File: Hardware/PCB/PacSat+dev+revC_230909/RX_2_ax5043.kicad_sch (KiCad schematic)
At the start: 15 parts, among them U151 RFShield_OnePiece, U305 AX5043

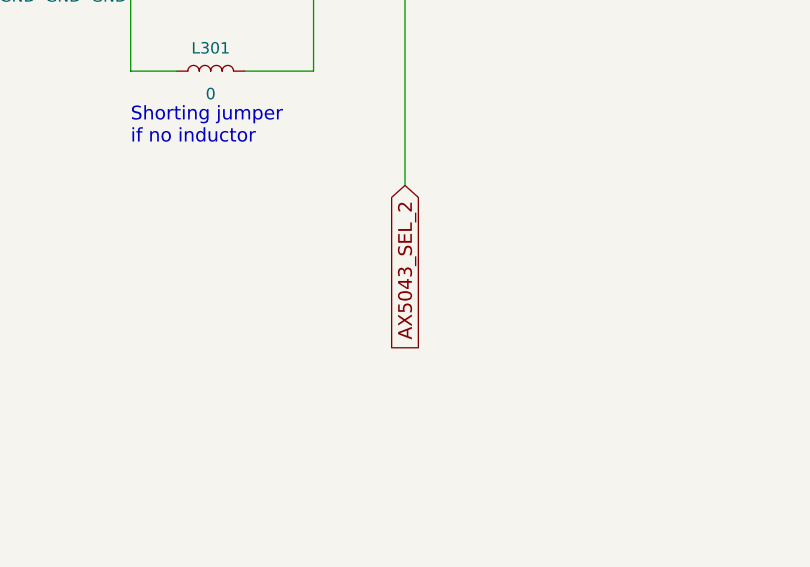
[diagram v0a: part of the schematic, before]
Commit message: Changed schematic to add Select lines for each AX5043 on the CPU.
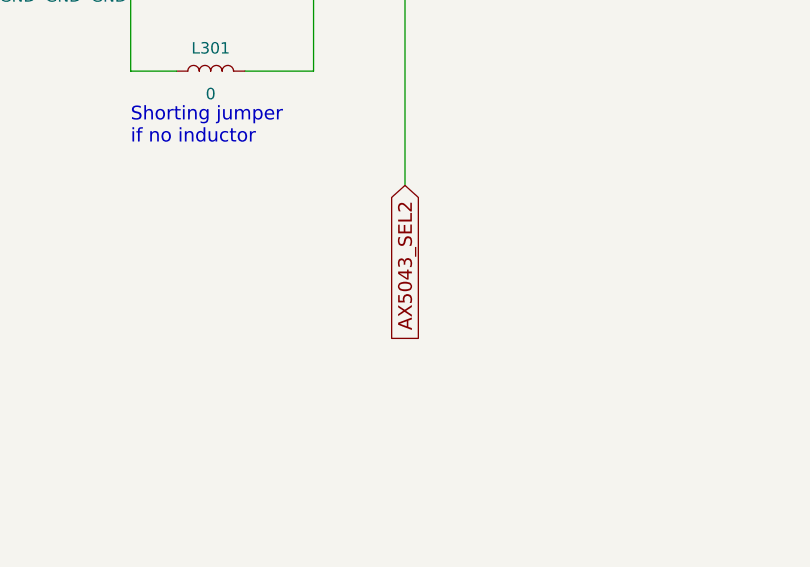
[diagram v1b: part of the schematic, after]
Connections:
- net AX5043_SEL_2 renamed AX5043_SEL2
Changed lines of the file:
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@@
     )
   )
-  (global_label "AX5043_SEL_2" (shape input) (at 226.06 181.61 270) (fields_autoplaced)
+  (global_label "AX5043_SEL2" (shape input) (at 226.06 181.61 270) (fields_autoplaced)
     (effects (font (size 1.524 1.524)) (justify right))
-    (property "Intersheetrefs" "${INTERSHEET_REFS}" (at 226.06 200.7123 90)
+    (property "Intersheetrefs" "${INTERSHEET_REFS}" (at 226.06 199.6466 90)
       (effects (font (size 1.524 1.524)) (justify right) hide)
     )
@@
     (pin "2")
     (instances
-      (project "pACsAT_dEV_rEVc_230907"
+      (project "PacSat+dev+revC_230909"
         (path "/cc9f42d2-6985-41ac-acab-5ab7b01c5b38/00000000-0000-0000-0000-00005a014be3"
           (reference "C712") (unit 1)
@@
     (pin "1")
     (instances
-      (project "pACsAT_dEV_rEVc_230907"
+      (project "PacSat+dev+revC_230909"
         (path "/cc9f42d2-6985-41ac-acab-5ab7b01c5b38/07d62cf1-e888-4b13-86c4-67d770627579"
           (reference "#PWR0191") (unit 1)
@@
     (pin "2")
     (instances
-      (project "pACsAT_dEV_rEVc_230907"
+      (project "PacSat+dev+revC_230909"
         (path "/cc9f42d2-6985-41ac-acab-5ab7b01c5b38/1e7123c2-80dc-43cd-b90a-12f3fe1af0cb"
           (reference "R303") (unit 1)
@@
     (pin "1")
     (instances
-      (project "pACsAT_dEV_rEVc_230907"
+      (project "PacSat+dev+revC_230909"
         (path "/cc9f42d2-6985-41ac-acab-5ab7b01c5b38/1e7123c2-80dc-43cd-b90a-12f3fe1af0cb"
           (reference "#PWR0304") (unit 1)
@@
     (pin "5")
     (instances
-      (project "pACsAT_dEV_rEVc_230907"
+      (project "PacSat+dev+revC_230909"
         (path "/cc9f42d2-6985-41ac-acab-5ab7b01c5b38/00000000-0000-0000-0000-00005a014be3"
           (reference "U151") (unit 1)
@@
     (pin "1")
     (instances
-      (project "pACsAT_dEV_rEVc_230907"
+      (project "PacSat+dev+revC_230909"
         (path "/cc9f42d2-6985-41ac-acab-5ab7b01c5b38/00000000-0000-0000-0000-00005a014be3"
           (reference "#PWR0161") (unit 1)
@@
     (pin "2")
     (instances
-      (project "pACsAT_dEV_rEVc_230907"
+      (project "PacSat+dev+revC_230909"
         (path "/cc9f42d2-6985-41ac-acab-5ab7b01c5b38/00000000-0000-0000-0000-00005a014be3"
           (reference "C711") (unit 1)
@@
     (pin "2")
     (instances
-      (project "pACsAT_dEV_rEVc_230907"
+      (project "PacSat+dev+revC_230909"
         (path "/cc9f42d2-6985-41ac-acab-5ab7b01c5b38/1e7123c2-80dc-43cd-b90a-12f3fe1af0cb"
           (reference "C303") (unit 1)
@@
     (pin "2")
     (instances
-      (project "pACsAT_dEV_rEVc_230907"
+      (project "PacSat+dev+revC_230909"
         (path "/cc9f42d2-6985-41ac-acab-5ab7b01c5b38/1e7123c2-80dc-43cd-b90a-12f3fe1af0cb"
           (reference "C304") (unit 1)
@@
     (pin "2")
     (instances
-      (project "pACsAT_dEV_rEVc_230907"
+      (project "PacSat+dev+revC_230909"
         (path "/cc9f42d2-6985-41ac-acab-5ab7b01c5b38/1e7123c2-80dc-43cd-b90a-12f3fe1af0cb"
           (reference "C307") (unit 1)
@@
     (pin "3")
     (instances
-      (project "pACsAT_dEV_rEVc_230907"
+      (project "PacSat+dev+revC_230909"
         (path "/cc9f42d2-6985-41ac-acab-5ab7b01c5b38/9af0eacb-5211-4e23-85d7-9c1805bbe6a4"
           (reference "U607") (unit 1)
@@
     (pin "1")
     (instances
-      (project "pACsAT_dEV_rEVc_230907"
+      (project "PacSat+dev+revC_230909"
         (path "/cc9f42d2-6985-41ac-acab-5ab7b01c5b38/1e7123c2-80dc-43cd-b90a-12f3fe1af0cb"
           (reference "#PWR0309") (unit 1)
@@
     (pin "1")
     (instances
-      (project "pACsAT_dEV_rEVc_230907"
+      (project "PacSat+dev+revC_230909"
         (path "/cc9f42d2-6985-41ac-acab-5ab7b01c5b38/1e7123c2-80dc-43cd-b90a-12f3fe1af0cb"
           (reference "#PWR0308") (unit 1)
@@
     (pin "1")
     (instances
-      (project "pACsAT_dEV_rEVc_230907"
+      (project "PacSat+dev+revC_230909"
         (path "/cc9f42d2-6985-41ac-acab-5ab7b01c5b38/00000000-0000-0000-0000-00005a014be3"
           (reference "#PWR0735") (unit 1)
@@
     (pin "1")
     (instances
-      (project "pACsAT_dEV_rEVc_230907"
+      (project "PacSat+dev+revC_230909"
         (path "/cc9f42d2-6985-41ac-acab-5ab7b01c5b38/1e7123c2-80dc-43cd-b90a-12f3fe1af0cb"
           (reference "#PWR0312") (unit 1)
@@
     (pin "2")
     (instances
-      (project "pACsAT_dEV_rEVc_230907"
+      (project "PacSat+dev+revC_230909"
         (path "/cc9f42d2-6985-41ac-acab-5ab7b01c5b38/1e7123c2-80dc-43cd-b90a-12f3fe1af0cb"
           (reference "C301") (unit 1)
@@
     (pin "9")
     (instances
-      (project "pACsAT_dEV_rEVc_230907"
+      (project "PacSat+dev+revC_230909"
         (path "/cc9f42d2-6985-41ac-acab-5ab7b01c5b38/1e7123c2-80dc-43cd-b90a-12f3fe1af0cb"
           (reference "U305") (unit 1)
@@
     (pin "1")
     (instances
-      (project "pACsAT_dEV_rEVc_230907"
+      (project "PacSat+dev+revC_230909"
         (path "/cc9f42d2-6985-41ac-acab-5ab7b01c5b38/1e7123c2-80dc-43cd-b90a-12f3fe1af0cb"
           (reference "#PWR0311") (unit 1)
@@
     (pin "3")
     (instances
-      (project "pACsAT_dEV_rEVc_230907"
+      (project "PacSat+dev+revC_230909"
         (path "/cc9f42d2-6985-41ac-acab-5ab7b01c5b38/9af0eacb-5211-4e23-85d7-9c1805bbe6a4"
           (reference "U605") (unit 1)
@@
     (pin "2")
     (instances
-      (project "pACsAT_dEV_rEVc_230907"
+      (project "PacSat+dev+revC_230909"
         (path "/cc9f42d2-6985-41ac-acab-5ab7b01c5b38/1e7123c2-80dc-43cd-b90a-12f3fe1af0cb"
           (reference "C302") (unit 1)
@@
     (pin "1")
     (instances
-      (project "pACsAT_dEV_rEVc_230907"
+      (project "PacSat+dev+revC_230909"
         (path "/cc9f42d2-6985-41ac-acab-5ab7b01c5b38/07d62cf1-e888-4b13-86c4-67d770627579"
           (reference "#PWR0191") (unit 1)
@@
     (pin "1")
     (instances
-      (project "pACsAT_dEV_rEVc_230907"
+      (project "PacSat+dev+revC_230909"
         (path "/cc9f42d2-6985-41ac-acab-5ab7b01c5b38/1e7123c2-80dc-43cd-b90a-12f3fe1af0cb"
           (reference "#PWR0305") (unit 1)
@@
     (pin "1")
     (instances
-      (project "pACsAT_dEV_rEVc_230907"
+      (project "PacSat+dev+revC_230909"
         (path "/cc9f42d2-6985-41ac-acab-5ab7b01c5b38/9af0eacb-5211-4e23-85d7-9c1805bbe6a4"
           (reference "#PWR0614") (unit 1)
@@
     (pin "2")
     (instances
-      (project "pACsAT_dEV_rEVc_230907"
+      (project "PacSat+dev+revC_230909"
         (path "/cc9f42d2-6985-41ac-acab-5ab7b01c5b38/07d62cf1-e888-4b13-86c4-67d770627579"
           (reference "R88") (unit 1)
@@
     (pin "2")
     (instances
-      (project "pACsAT_dEV_rEVc_230907"
+      (project "PacSat+dev+revC_230909"
         (path "/cc9f42d2-6985-41ac-acab-5ab7b01c5b38/1e7123c2-80dc-43cd-b90a-12f3fe1af0cb"
           (reference "R302") (unit 1)
@@
     (pin "1")
     (instances
-      (project "pACsAT_dEV_rEVc_230907"
+      (project "PacSat+dev+revC_230909"
         (path "/cc9f42d2-6985-41ac-acab-5ab7b01c5b38/1e7123c2-80dc-43cd-b90a-12f3fe1af0cb"
           (reference "#PWR0306") (unit 1)
@@
     (pin "2")
     (instances
-      (project "pACsAT_dEV_rEVc_230907"
+      (project "PacSat+dev+revC_230909"
         (path "/cc9f42d2-6985-41ac-acab-5ab7b01c5b38/1e7123c2-80dc-43cd-b90a-12f3fe1af0cb"
           (reference "L301") (unit 1)
